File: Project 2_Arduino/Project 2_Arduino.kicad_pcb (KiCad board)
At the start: 2 copper layers, 29 parts, among them J10 Conn_01x08, J11 Conn_01x08, J12 Conn_01x06, J13 Conn_01x03, J3 USB_microB_2040002-1, J4 Conn_02x03_Odd_Even, SW1 SW_Push, U1 FT232RL, U3 ATMEGA328P-AU, Y1 16MHz

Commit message: finished layout
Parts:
- Y1: value 16MHz -> Crystal_GND24
- moved C3 52.1 mm to (143.3, 91.4), turned to 180 degrees
- moved C7 49.8 mm to (143.3, 96.0), turned to 180 degrees
- moved C5 49.7 mm to (143.3, 93.7), turned to 180 degrees
- moved C9 43.5 mm to (148.2, 91.4), turned to 180 degrees
- moved R3 43.2 mm to (144.1, 112.3), turned to 90 degrees
- moved DX1 41.4 mm to (144.1, 115.7), turned to 270 degrees
- moved C6 39.8 mm to (143.3, 102.1), turned to 270 degrees
- moved DX2 38.2 mm to (146.3, 115.7), turned to 270 degrees
- moved R4 32.8 mm to (146.2, 112.3), turned to 90 degrees
- moved J13 32.0 mm to (140.8, 104.1), turned to 180 degrees
- moved R2 30.5 mm to (156.7, 104.3)
- moved R6 30.1 mm to (161.0, 116.8)
- moved SW1 28.2 mm to (173.2, 92.2), turned to 180 degrees
- moved C4 26.9 mm to (160.8, 115.3)
- moved D3 25.7 mm to (174.4, 108.6), turned to 90 degrees
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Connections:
- U3 pad 7: GND -> Net-(U3-Pad7)
- U3 pad 8: GND -> Net-(U3-Pad8)
- Y1 pad 1: GND -> Net-(U3-Pad7)
- Y1 pad 3: (no net) -> Net-(U3-Pad8)
- Y1 pad 4: (no net) -> GND
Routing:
- net RESET: track 0.00 -> 45.8 mm, vias 0 -> 2
- net D7: track 0.00 -> 24.2 mm, vias 0 -> 1
- net D6: track 0.00 -> 24.2 mm, vias 0 -> 1
- net D5: track 0.00 -> 23.8 mm, vias 0 -> 1
- net D1/TX: track 0.00 -> 21.0 mm, vias 0 -> 2
- net D12/MISO: track 0.00 -> 19.4 mm, vias 0 -> 1
- net D13/SCK: track 0.00 -> 19.2 mm, vias 0 -> 1
- net Net-(U3-Pad8): track 0.00 -> 17.2 mm
- net D11/MOSI: track 0.00 -> 16.1 mm, vias 0 -> 1
- net D4: track 0.00 -> 15.5 mm, vias 0 -> 1
- net D0/RX: track 0.00 -> 14.9 mm
- net D8: track 0.00 -> 14.1 mm
- net D3: track 0.00 -> 13.9 mm, vias 0 -> 1
- net A6: track 0.00 -> 13.3 mm, vias 0 -> 1
- net D9: track 0.00 -> 12.9 mm
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- added copper zone on B.Cu, net 5V
- added copper zone on F.Cu, net GND
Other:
- board outline added: 39.2 x 31.5 mm

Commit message: fixed flows
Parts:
- moved C6 0.85 mm to (142.9, 101.3), turned to 90 degrees
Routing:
- net GND: track 0.00 -> 33.5 mm, vias 0 -> 2
- net 5V: track 9.68 -> 37.9 mm, vias 3 -> 8
- net (no net): track 0.00 -> 6.17 mm, vias 0 -> 4

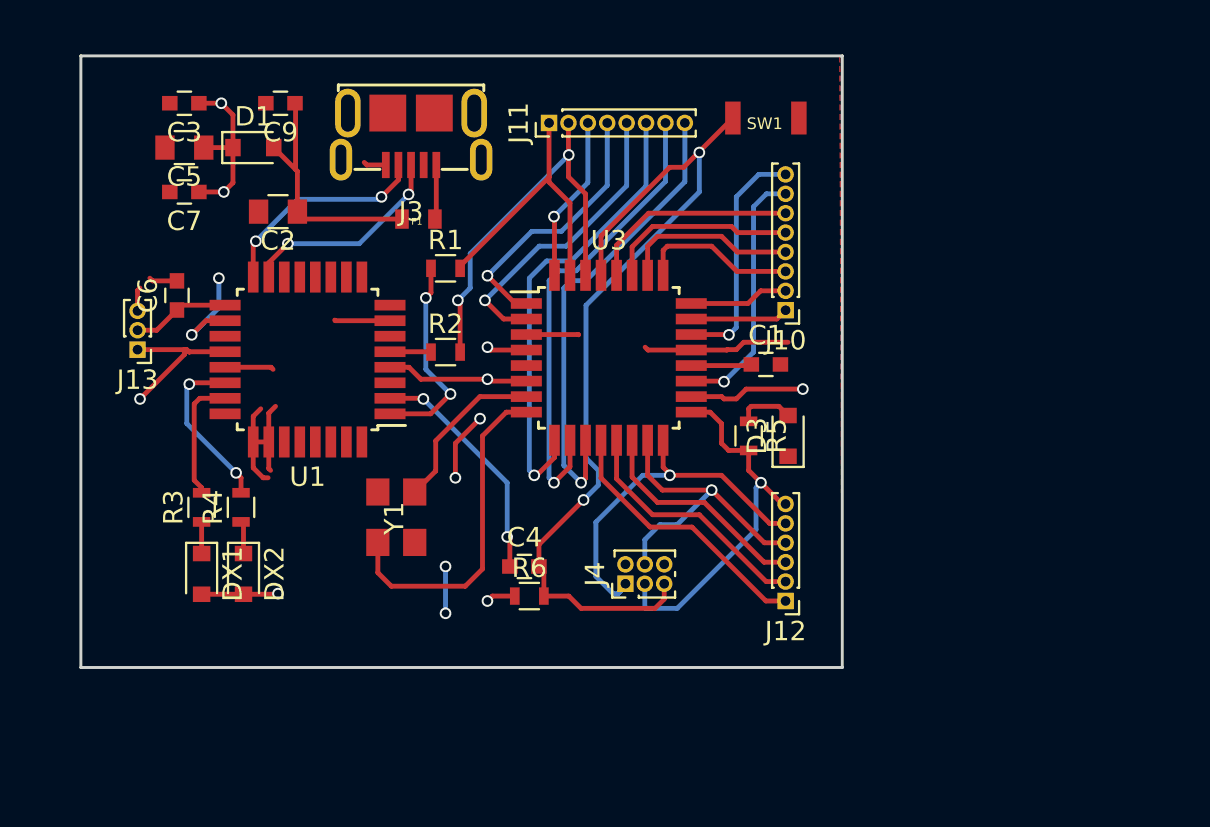
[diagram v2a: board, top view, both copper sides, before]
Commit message: connections and USB location fixed
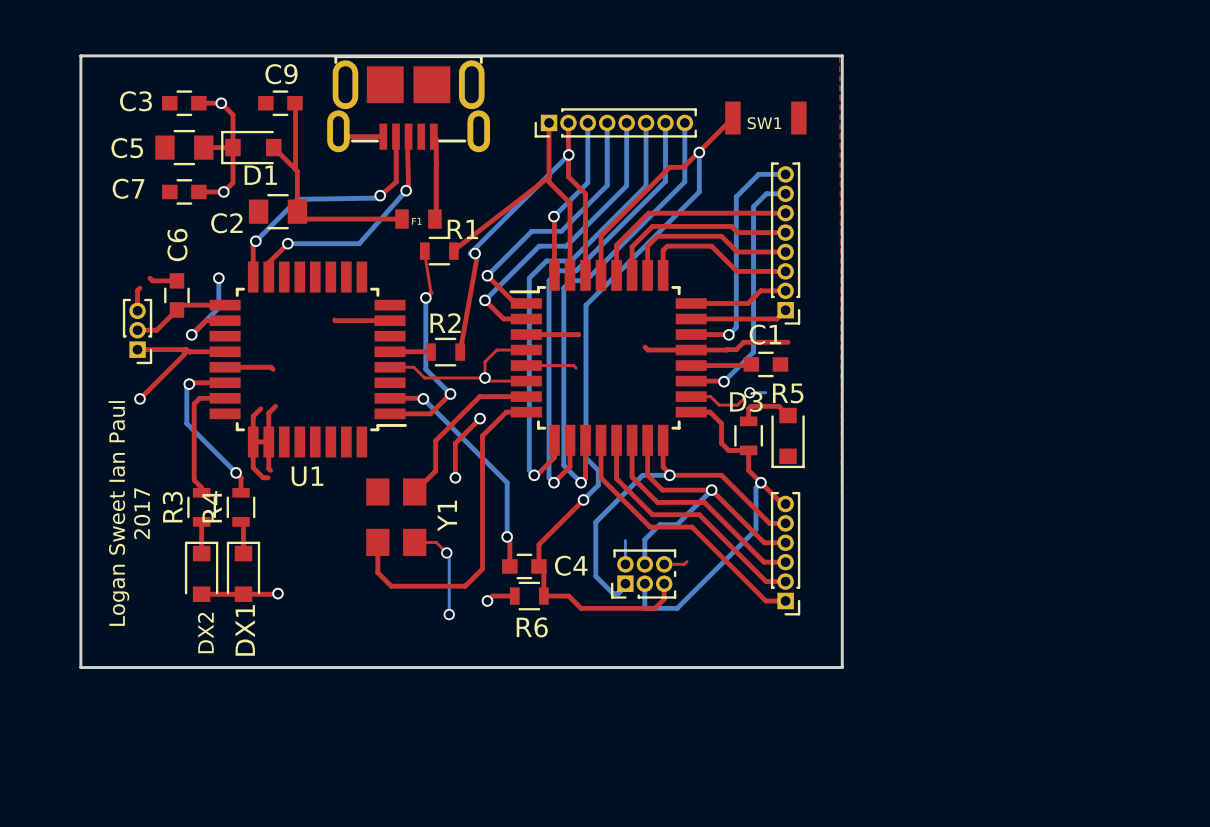
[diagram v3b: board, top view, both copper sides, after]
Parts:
- moved J3 1.47 mm to (154.8, 90.5)
- moved R1 0.94 mm to (156.4, 99.1)
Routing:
- net GND: track 33.5 -> 43.7 mm, vias 2 -> 4
- net (no net): track 6.17 -> 3.75 mm, vias 4 -> 2
- net Net-(F1-Pad1): track 2.81 -> 4.33 mm
- net Net-(J3-Pad4): track 11.3 -> 12.7 mm
- net Net-(J3-Pad3): track 11.0 -> 12.2 mm
- net RX: track 10.7 -> 11.5 mm
- net 5V: track 37.9 -> 38.5 mm, vias 8 -> 7
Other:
- net class Default: trace_width 0.25 -> 0.1525
- board text added: "Logan Sweet Ian Paul 2017"
